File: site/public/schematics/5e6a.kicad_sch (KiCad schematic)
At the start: 62 parts, among them T3 part not legible

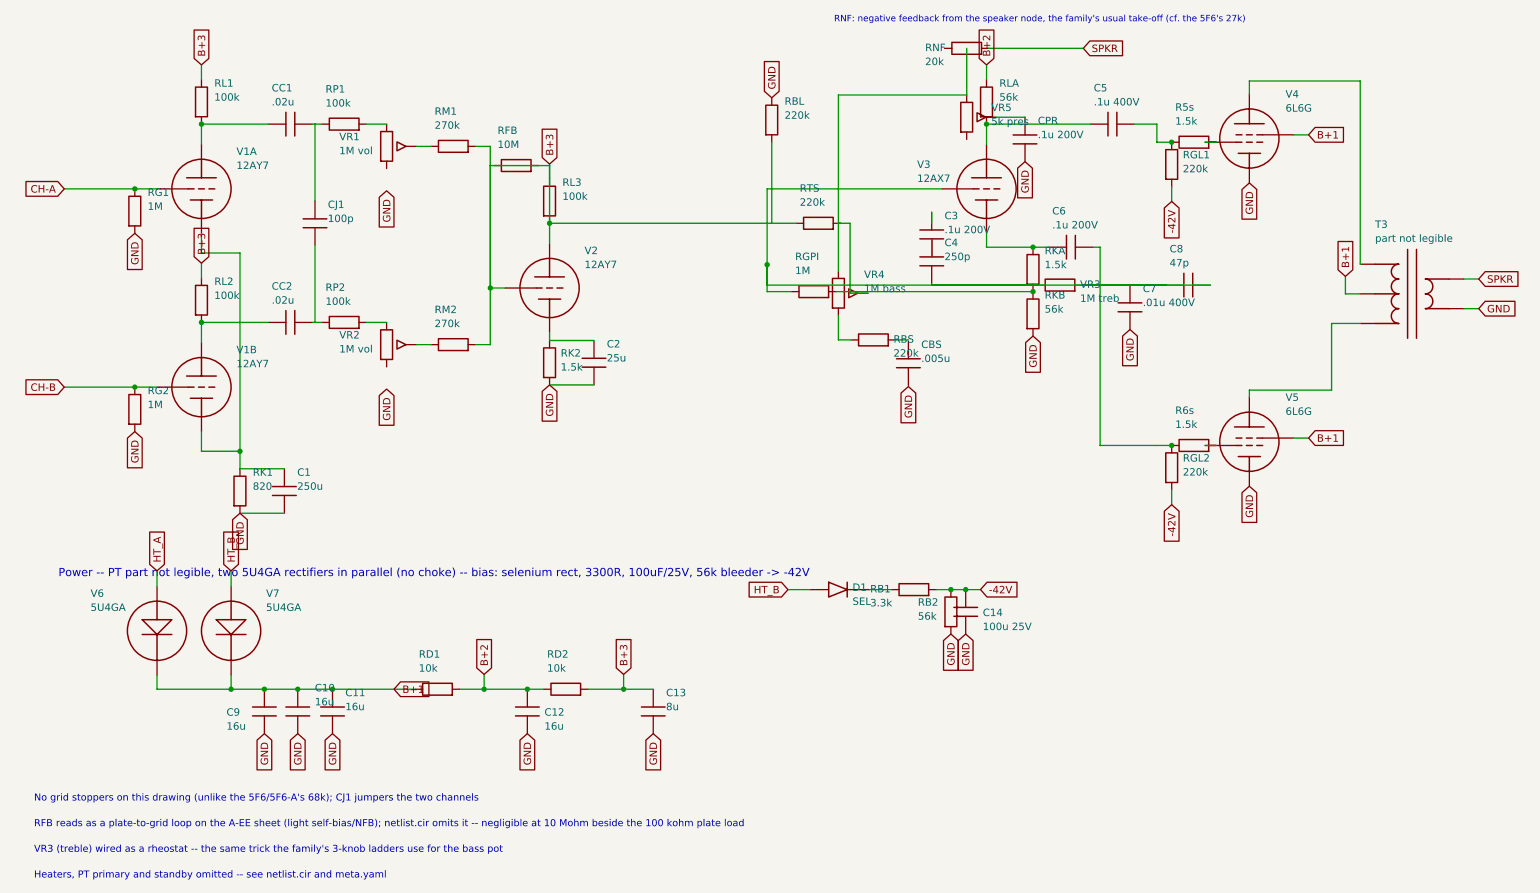
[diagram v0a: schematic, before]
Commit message: Fix: site copies of 29 sheets re-synced; regenerate step syncs before the drift check
- the drawing scripts write amps/; site/public/schematics is refreshed by
  site/scripts/sync-assets.mjs, which CI only ran inside the site build, so
  the fixer commits carried stale copies and the new drift gate caught them
- CI now syncs immediately after regenerating and diffs both trees; the
  AGENTS.md regenerate command does the same

Co-Authored-By: Claude Fable 5.1 <noreply@anthropic.com>
Claude-Session: https://claude.ai/code/session_01KBMfdh37HmCL2iWcBiL5J1
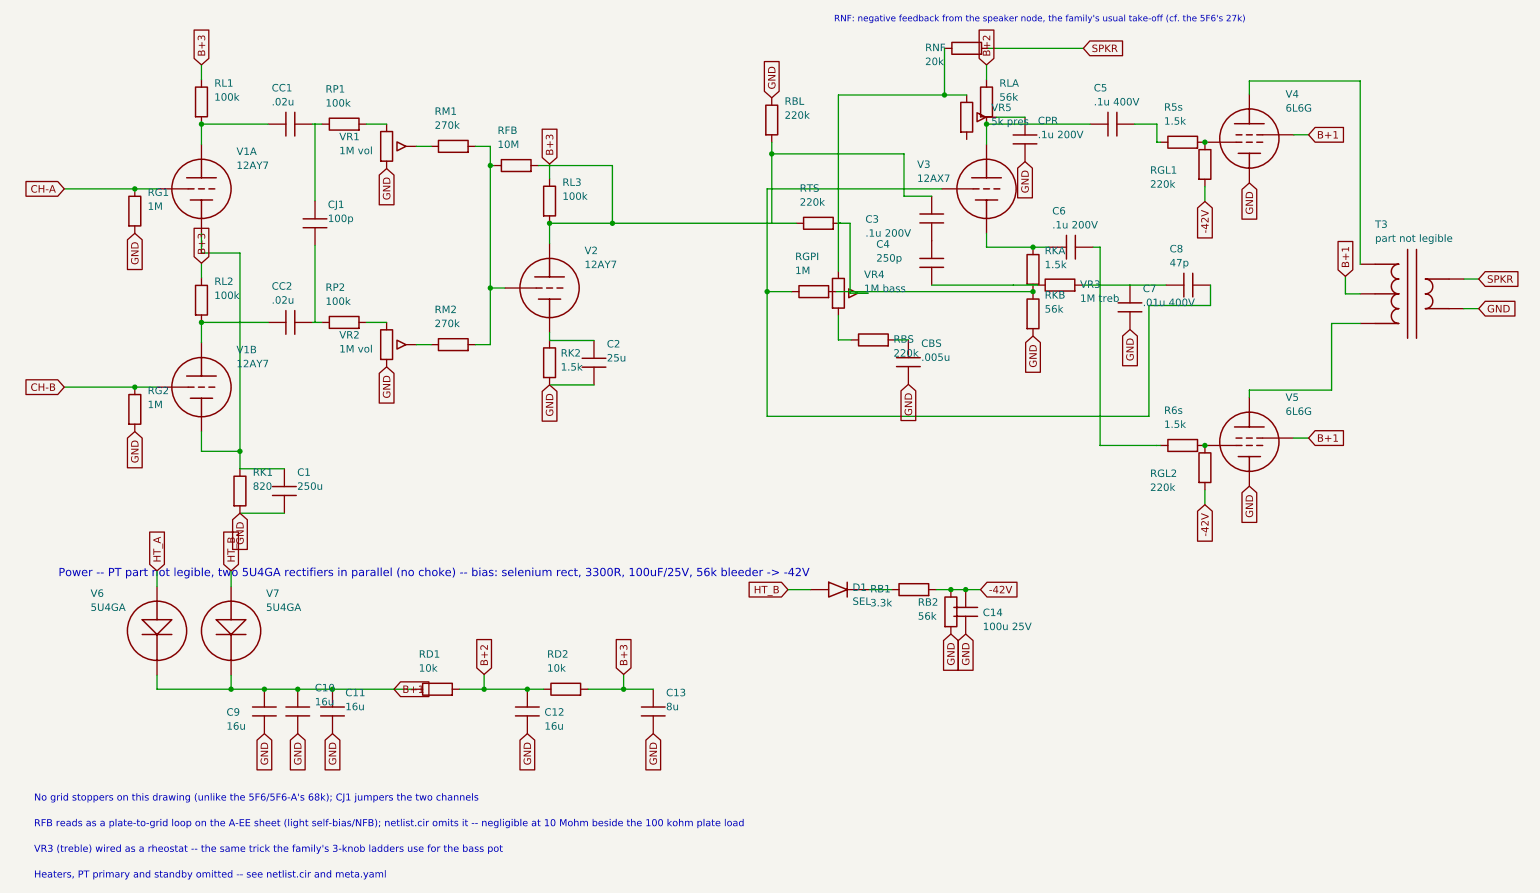
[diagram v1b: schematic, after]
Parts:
- removed C3: .1u 200V, symbol cx:C
- removed D1: SEL, symbol cx:DIODE_SS
- removed RGL1, RGL2: 220k, symbol cx:R
- removed V7: 5U4GA, symbol cx:DIODE_TUBE
- added C13: 8u, symbol cx:C
- added C7: .01u 400V, symbol cx:C
- added R6s: 1.5k, symbol cx:R
- added V4: 6L6G, symbol cx:PENTODE
- added V6: 5U4GA, symbol cx:DIODE_TUBE
- C3: renamed from VR3; value 1M treb -> .1u 200V; symbol cx:R -> cx:C
- D1: renamed from C13; value 8u -> SEL; symbol cx:C -> cx:DIODE_SS
- RGL1: renamed from V4; value 6L6G -> 220k; symbol cx:PENTODE -> cx:R
- RGL2: renamed from R6s; value 1.5k -> 220k
- VR3: renamed from C7; value .01u 400V -> 1M treb; symbol cx:C -> cx:R
- renumbered V6 to V7
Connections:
- net -42V: now also RGL1.2, RGL2.2
- net B+1: now also V4.3 (G2), V6.2 (K); no longer RGL1.3 (G2)
- net B+3: now also C13.1; no longer D1.1, RBL.2, RFB.1, RFB.2, RL3.2, RM1.2, RM2.2, RTS.1, V2.1 (P)
- net GND: now also CBS.2, VR1.3, VR2.3, C13.2, C7.2, V4.4 (K); no longer D1.2, RGL1.4 (K), VR3.2
- net HT_A: now also V6.1 (A); no longer V7.1 (A)
- net HT_B: now also D1.1 (A), V7.1 (A)
- net at CBS.1: now also RBS.2
- net at RTS.2, VR4.1, VR4.2 (W)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: now also RNF.1
- net at RGL2.1: now also V5.2 (G1), R6s.2; no longer C6.2
- net at RB1.1: now also D1.2 (K)
- net at RGL1.1: now also R5s.2, V4.2 (G1); no longer T3.1 (PRI_A)
- net at C4.1: now also C3.2
- new net: C6.2, R6s.1
- new net: C8.2, RGPI.1, V3.2 (G)
- new net: RFB.1, RM1.2, RM2.2
- new net: C3.1, RBL.2, RFB.2, RL3.2, RTS.1, V2.1 (P)
- new net: T3.1 (PRI_A), V4.1 (P)
- new net: C7.1, C8.1, VR3.2
- new net: C4.2, VR3.1
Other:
- moved on the sheet: D1, RGL2, V7
